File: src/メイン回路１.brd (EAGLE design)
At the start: 35 parts, among them T1 一般的なトランジスタ, T2 一般的なトランジスタ, T3 一般的なトランジスタ, T4 一般的なトランジスタ

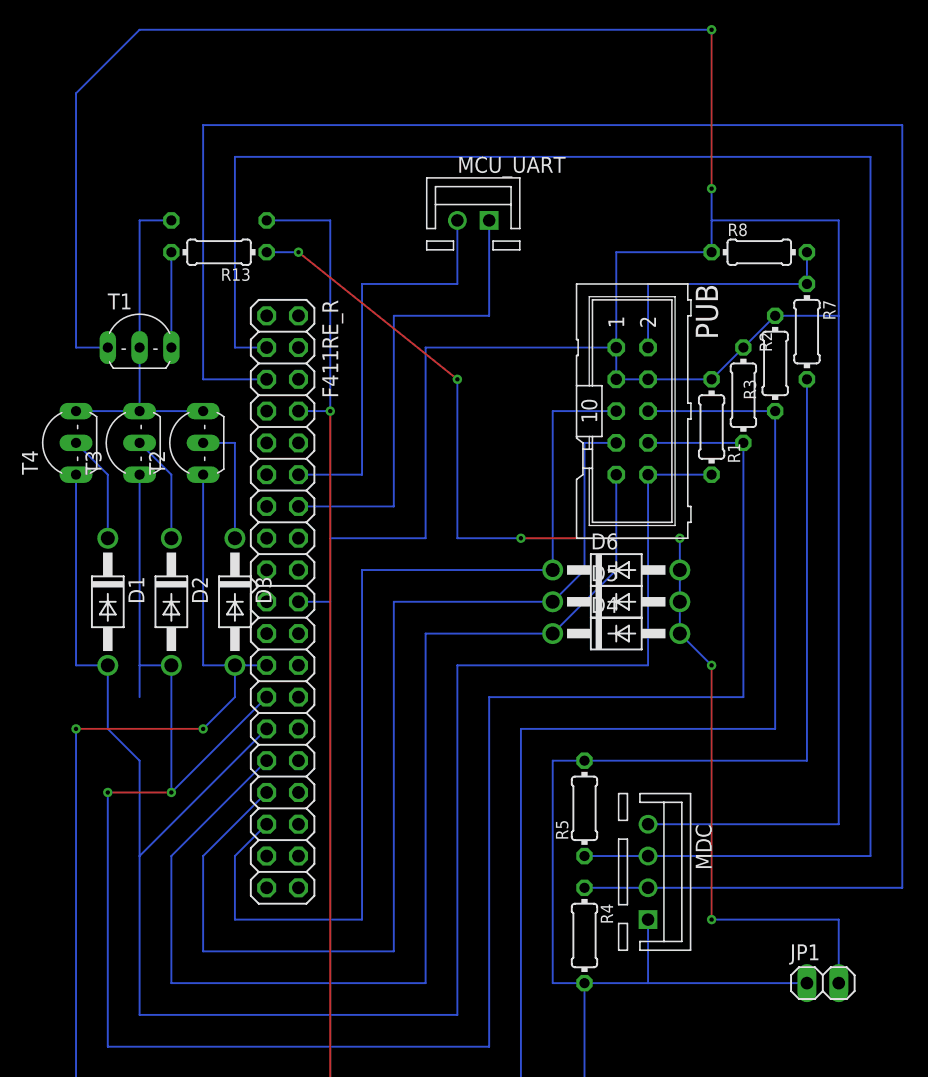
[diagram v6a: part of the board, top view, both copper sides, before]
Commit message: [add]メイン回路1にソケット置きを追加
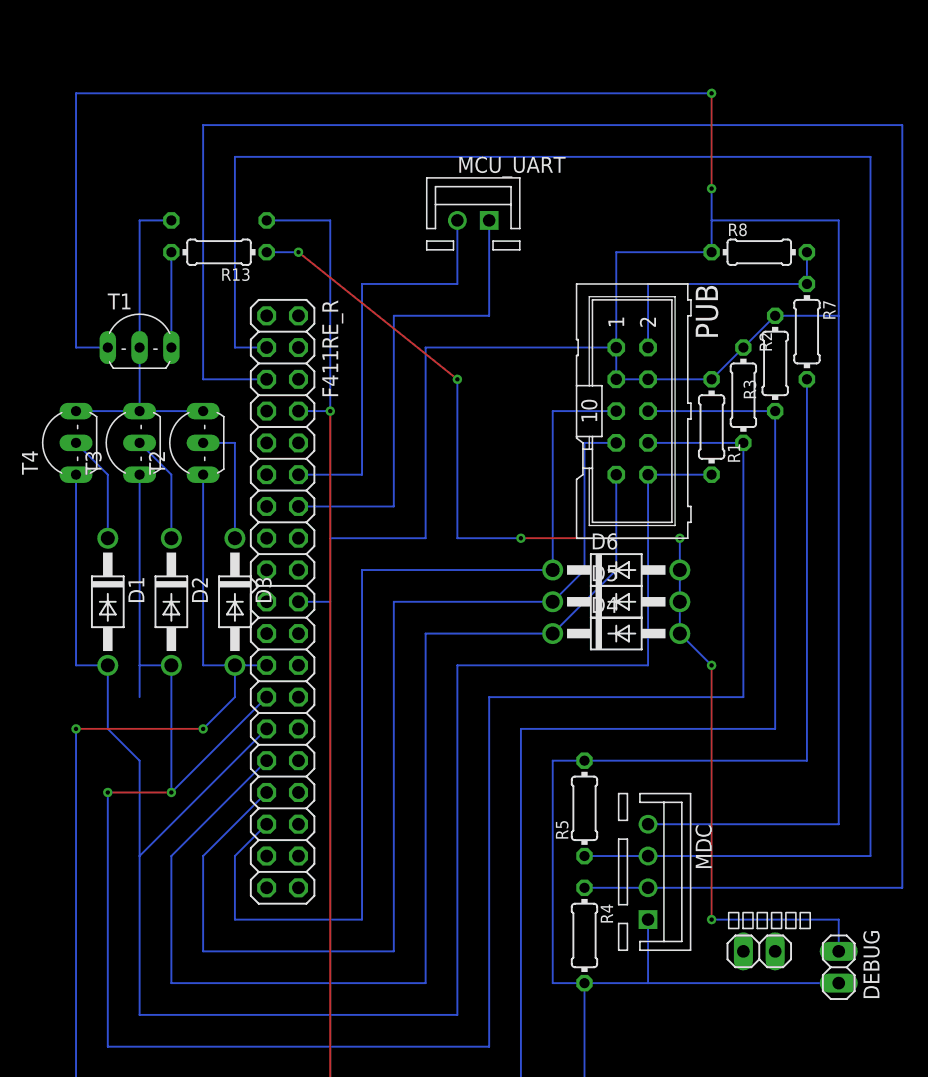
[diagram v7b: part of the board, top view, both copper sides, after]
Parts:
- removed JP1: (no value), pinhead:1X02
- added DEBUG, ソケット置き: (no value), pinhead:1X02
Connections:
- net DEBUG: now also DEBUG.2; no longer JP1.2
- net U5V: now also DEBUG.1; no longer JP1.1
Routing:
- net GND: track 359.8 -> 352.6 mm
- net DEBUG: track 96.1 -> 93.5 mm
- net U5V: track 203.2 -> 205.7 mm
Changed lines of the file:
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@@
 <element name="U$1" library="prototyping-board" package="TYPE.B" value="" x="55.88" y="-15.24" smashed="yes" rot="R90"/>
 <element name="U$2" library="prototyping-board" package="TYPE.B" value="" x="132.08" y="-15.24" smashed="yes" rot="R90"/>
-<element name="JP1" library="pinhead" library_urn="urn:adsk.eagle:library:325" package="1X02" package3d_urn="urn:adsk.eagle:package:22435/2" value="" x="123.19" y="0" smashed="yes">
-<attribute name="NAME" x="120.5738" y="1.8288" size="1.27" layer="25" ratio="10"/>
-<attribute name="POPULARITY" value="98" x="123.19" y="0" size="1.778" layer="27" display="off"/>
-<attribute name="VALUE" x="120.65" y="-3.175" size="1.27" layer="27"/>
+<element name="DEBUG" library="pinhead" library_urn="urn:adsk.eagle:library:325" package="1X02" package3d_urn="urn:adsk.eagle:package:22435/2" value="" x="124.46" y="1.27" smashed="yes" rot="R90">
+<attribute name="NAME" x="127.7112" y="-1.3462" size="1.27" layer="25" ratio="10" rot="R90"/>
+<attribute name="POPULARITY" value="98" x="124.46" y="1.27" size="1.778" layer="27" rot="R90" display="off"/>
+<attribute name="VALUE" x="127.635" y="-1.27" size="1.27" layer="27" rot="R90"/>
 </element>
 <element name="R13" library="rcl" library_urn="urn:adsk.eagle:library:334" package="0204/7" package3d_urn="urn:adsk.eagle:package:23498/2" value="10k" x="74.93" y="58.42" smashed="yes" rot="R180">
@@
 <attribute name="NAME" x="60.452" y="40.64" size="1.27" layer="25" ratio="10" rot="R90"/>
 <attribute name="VALUE" x="66.802" y="40.64" size="1.27" layer="27" ratio="10" rot="R90"/>
+</element>
+<element name="ソケット置き" library="pinhead" library_urn="urn:adsk.eagle:library:325" package="1X02" package3d_urn="urn:adsk.eagle:package:22435/2" value="" x="118.11" y="2.54" smashed="yes">
+<attribute name="NAME" x="115.4938" y="4.3688" size="1.27" layer="25" ratio="10"/>
+<attribute name="POPULARITY" value="98" x="118.11" y="2.54" size="1.778" layer="27" display="off"/>
+<attribute name="VALUE" x="115.57" y="-0.635" size="1.27" layer="27"/>
 </element>
 </elements>
@@
 <wire x1="66.04" y1="50.8" x2="63.5" y2="50.8" width="0.1524" layer="16"/>
 <wire x1="63.5" y1="50.8" x2="63.5" y2="71.12" width="0.1524" layer="16"/>
-<wire x1="63.5" y1="71.12" x2="68.58" y2="76.2" width="0.1524" layer="16"/>
-<wire x1="68.58" y1="76.2" x2="114.3" y2="76.2" width="0.1524" layer="16"/>
-<via x="114.3" y="76.2" extent="1-16" drill="0.35"/>
-<wire x1="114.3" y1="76.2" x2="114.3" y2="63.5" width="0.1524" layer="1"/>
+<wire x1="114.3" y1="71.12" x2="63.5" y2="71.12" width="0.1524" layer="16"/>
+<via x="114.3" y="71.12" extent="1-16" drill="0.35"/>
+<wire x1="114.3" y1="71.12" x2="114.3" y2="63.5" width="0.1524" layer="1"/>
 <via x="114.3" y="63.5" extent="1-16" drill="0.35"/>
 <wire x1="114.3" y1="63.5" x2="114.3" y2="60.96" width="0.1524" layer="16"/>
@@
 <wire x1="63.5" y1="25.4" x2="63.5" y2="40.64" width="0.1524" layer="16"/>
 <wire x1="78.74" y1="20.32" x2="68.58" y2="10.16" width="0.1524" layer="16"/>
+<wire x1="68.58" y1="17.78" x2="68.58" y2="10.16" width="0.1524" layer="16"/>
 <wire x1="66.04" y1="20.32" x2="68.58" y2="17.78" width="0.1524" layer="16"/>
-<wire x1="68.58" y1="17.78" x2="68.58" y2="10.16" width="0.1524" layer="16"/>
 </signal>
 <signal name="SDA">
@@
 <wire x1="83.82" y1="-10.16" x2="104.14" y2="-10.16" width="0.1524" layer="16"/>
 <wire x1="104.14" y1="-10.16" x2="104.14" y2="0" width="0.1524" layer="16"/>
-<contactref element="JP1" pad="1"/>
+<contactref element="DEBUG" pad="1"/>
 <contactref element="R14" pad="2"/>
-<wire x1="121.92" y1="0" x2="109.22" y2="0" width="0.1524" layer="16"/>
+<wire x1="124.46" y1="0" x2="109.22" y2="0" width="0.1524" layer="16"/>
 <wire x1="78.74" y1="60.96" x2="83.82" y2="60.96" width="0.1524" layer="16"/>
 <wire x1="83.82" y1="60.96" x2="83.82" y2="45.72" width="0.1524" layer="16"/>
@@
 </signal>
 <signal name="DEBUG">
-<contactref element="JP1" pad="2"/>
+<contactref element="DEBUG" pad="2"/>
 <contactref element="R13" pad="1"/>
 <contactref element="D4" pad="A"/>
@@
 <wire x1="111.76" y1="30.48" x2="111.76" y2="33.02" width="0.1524" layer="16"/>
 <wire x1="111.76" y1="30.48" x2="111.76" y2="27.94" width="0.1524" layer="16"/>
-<wire x1="124.46" y1="0" x2="124.46" y2="5.08" width="0.1524" layer="16"/>
+<wire x1="124.46" y1="2.54" x2="124.46" y2="5.08" width="0.1524" layer="16"/>
 <via x="114.3" y="25.4" extent="1-16" drill="0.35"/>
 <wire x1="114.3" y1="25.4" x2="111.76" y2="27.94" width="0.1524" layer="16"/>

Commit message: [fix]接続問題の解消
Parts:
- moved D1 17.7 mm to (72.4, 14.0), turned to 225 degrees
- moved D3 14.5 mm to (67.3, 19.1), turned to 225 degrees
- moved D2 14.0 mm to (69.8, 16.5), turned to 225 degrees
- moved T2 12.7 mm to (63.5, 35.6)
- moved T4 12.7 mm to (73.7, 35.6)
- moved T3 7.62 mm to (68.6, 35.6)
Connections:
- removed net N$5: D3.C, T2.C
- removed net N$6: D2.C, T3.C
- removed net N$7: D1.C, T4.C
- new net N$8: D1.A, PUB.10, R1.2, T4.E
- new net N$9: D2.A, PUB.8, R2.2, T3.E
- new net N$Q0: D3.A, PUB.6, R3.2, T2.E
- net PWM1: now also D1.C, T4.C; no longer D1.A, PUB.10, R1.2, T4.E
- net PWM2: now also D2.C, T3.C; no longer D2.A, PUB.8, R2.2, T3.E
- net PWM3: now also D3.C, T2.C; no longer D3.A, PUB.6, R3.2, T2.E
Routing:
- net N$Q0: track 0.00 -> 160.3 mm
- net PWM3: track 183.9 -> 23.8 mm
- net PWM2: track 173.3 -> 24.1 mm, vias 2 -> 4
- net N$9: track 0.00 -> 146.1 mm
- net PWM1: track 150.0 -> 22.7 mm, vias 0 -> 2
- net N$8: track 0.00 -> 123.7 mm
- net N$5: track 10.2 -> 0.00 mm
- net N$7: track 8.67 -> 0.00 mm
- net N$6: track 8.67 -> 0.00 mm
- net ZM: track 27.9 -> 35.6 mm
